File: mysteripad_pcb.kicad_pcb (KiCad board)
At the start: 2 copper layers, 76.2 x 146.6 mm, 74 parts, among them J1 PJ-320A, U1 ATmega328P-PU, Y1 Crystal

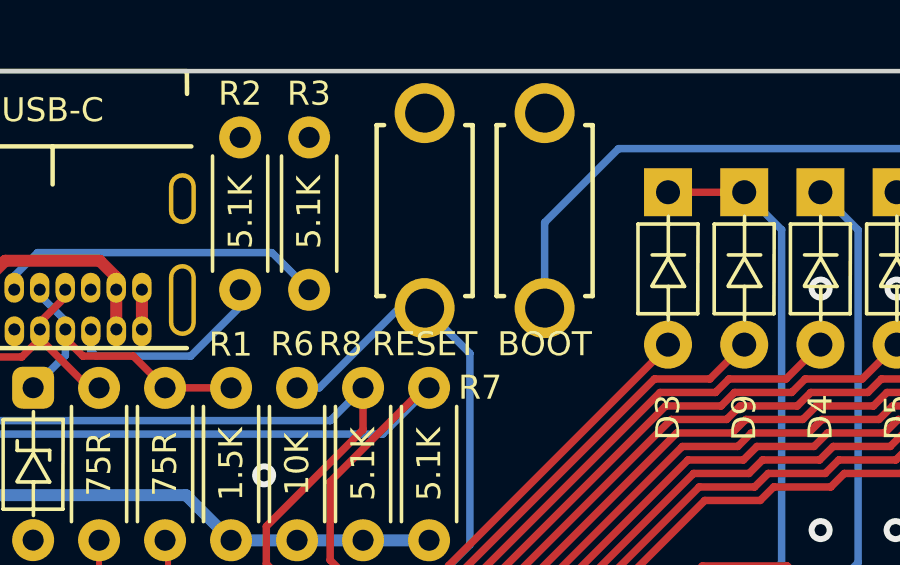
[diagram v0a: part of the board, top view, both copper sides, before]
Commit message: Fix RESET/BOOT silkscreen
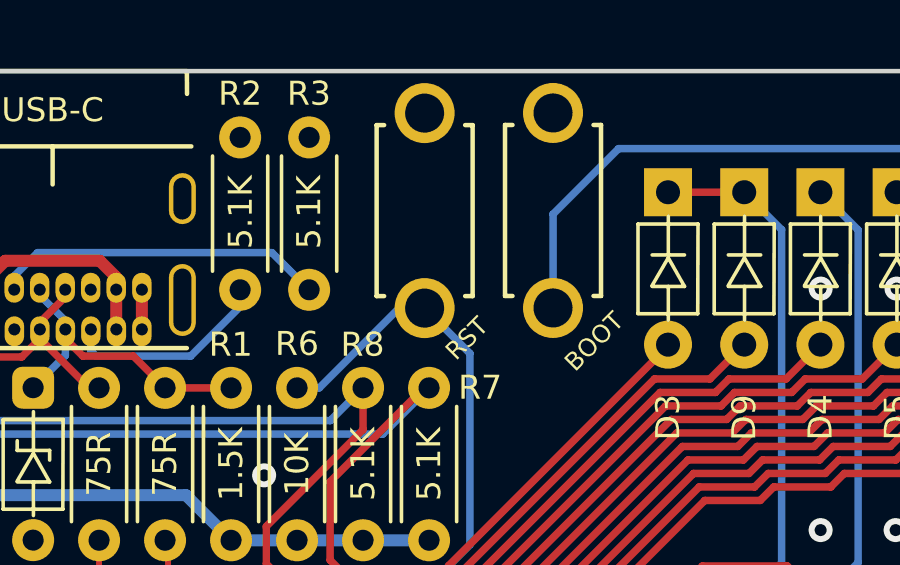
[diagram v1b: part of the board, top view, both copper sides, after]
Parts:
- RESET1: value RESET -> RST
- moved BOOT1 0.28 mm to (113.0, 34.6)
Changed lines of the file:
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@@
       (effects (font (size 1 1) (thickness 0.15)))
     )
-    (fp_text value "RESET" (at -4.45 0 180) (layer "F.SilkS")
-      (effects (font (size 0.8 0.8) (thickness 0.15)))
+    (fp_text value "RST" (at -4.2628 1.4098 225) (layer "F.SilkS")
+      (effects (font (size 0.6 0.6) (thickness 0.15)))
     )
     (fp_text user "RESET" (at 0 0 90) (layer "F.SilkS") hide
@@
     (property "Sheetname" "")
     (attr through_hole)
-    (fp_text reference "R8" (at 6.53895 -0.7542) (layer "F.SilkS")
+    (fp_text reference "R8" (at 6.52295 -0.0176) (layer "F.SilkS")
       (effects (font (size 0.8 0.8) (thickness 0.15)))
     )
@@
   )
   (footprint "kbd:ResetSW_1side" (layer "F.Cu")
-    (at 112.75 34.65 90)
+    (at 113.03 34.6456 90)
     (property "Sheetfile" "mysteripad_pcb.kicad_sch")
     (property "Sheetname" "")
@@
       (effects (font (size 1 1) (thickness 0.15)))
     )
-    (fp_text value "BOOT" (at -4.45 0 180) (layer "F.SilkS")
-      (effects (font (size 0.8 0.8) (thickness 0.15)))
+    (fp_text value "BOOT" (at -4.3688 1.3716 225) (layer "F.SilkS")
+      (effects (font (size 0.6 0.6) (thickness 0.15)))
     )
     (fp_text user "RESET" (at 0 0 90) (layer "F.SilkS") hide
@@
     (property "Sheetname" "")
     (attr through_hole)
-    (fp_text reference "R6" (at 6.53895 -0.1566) (layer "F.SilkS")
+    (fp_text reference "R6" (at 6.54835 -0.002) (layer "F.SilkS")
       (effects (font (size 0.8 0.8) (thickness 0.15)))
     )
@@
   (segment (start 95.948008 49.2134) (end 102.931612 49.2134) (width 0.25) (layer "B.Cu") (net 2))
   (segment (start 95.472608 48.738) (end 95.948008 49.2134) (width 0.25) (layer "B.Cu") (net 2))
-  (segment (start 112.75 37.9) (end 112.75 35.05) (width 0.25) (layer "B.Cu") (net 2))
+  (segment (start 125.569399 32.583999) (end 127.023 34.0376) (width 0.25) (layer "B.Cu") (net 2))
   (segment (start 105.259816 49.638) (end 106.221816 50.6) (width 0.25) (layer "B.Cu") (net 2))
+  (segment (start 113.03 34.77) (end 115.216001 32.583999) (width 0.25) (layer "B.Cu") (net 2))
   (segment (start 128.3 35.3146) (end 128.3 46.362751) (width 0.25) (layer "B.Cu") (net 2))
   (segment (start 125.892151 48.7706) (end 127.041903 47.620848) (width 0.25) (layer "B.Cu") (net 2))
   (segment (start 123.988547 48.7706) (end 125.892151 48.7706) (width 0.25) (layer "B.Cu") (net 2))
   (segment (start 128.3 46.362751) (end 127.041903 47.620848) (width 0.25) (layer "B.Cu") (net 2))
-  (segment (start 115.216001 32.583999) (end 125.569399 32.583999) (width 0.25) (layer "B.Cu") (net 2))
   (segment (start 121.634943 49.2206) (end 123.538547 49.2206) (width 0.25) (layer "B.Cu") (net 2))
   (segment (start 121.184943 49.6706) (end 121.634943 49.2206) (width 0.25) (layer "B.Cu") (net 2))
-  (segment (start 125.569399 32.583999) (end 127.023 34.0376) (width 0.25) (layer "B.Cu") (net 2))
   (segment (start 106.221816 50.6) (end 118.351939 50.6) (width 0.25) (layer "B.Cu") (net 2))
   (segment (start 82.266004 47.595) (end 83.409004 48.738) (width 0.25) (layer "B.Cu") (net 2))
   (segment (start 119.281339 49.6706) (end 121.184943 49.6706) (width 0.25) (layer "B.Cu") (net 2))
-  (segment (start 112.75 35.05) (end 115.216001 32.583999) (width 0.25) (layer "B.Cu") (net 2))
   (segment (start 83.409004 48.738) (end 95.472608 48.738) (width 0.25) (layer "B.Cu") (net 2))
   (segment (start 123.538547 49.2206) (end 123.988547 48.7706) (width 0.25) (layer "B.Cu") (net 2))
   (segment (start 118.351939 50.6) (end 119.281339 49.6706) (width 0.25) (layer "B.Cu") (net 2))
   (segment (start 127.023 34.0376) (end 128.3 35.3146) (width 0.25) (layer "B.Cu") (net 2))
+  (segment (start 113.03 37.8956) (end 113.03 34.77) (width 0.25) (layer "B.Cu") (net 2))
+  (segment (start 115.216001 32.583999) (end 125.569399 32.583999) (width 0.25) (layer "B.Cu") (net 2))
   (segment (start 102.931612 49.2134) (end 103.356212 49.638) (width 0.25) (layer "B.Cu") (net 2))
   (segment (start 103.356212 49.638) (end 105.259816 49.638) (width 0.25) (layer "B.Cu") (net 2))

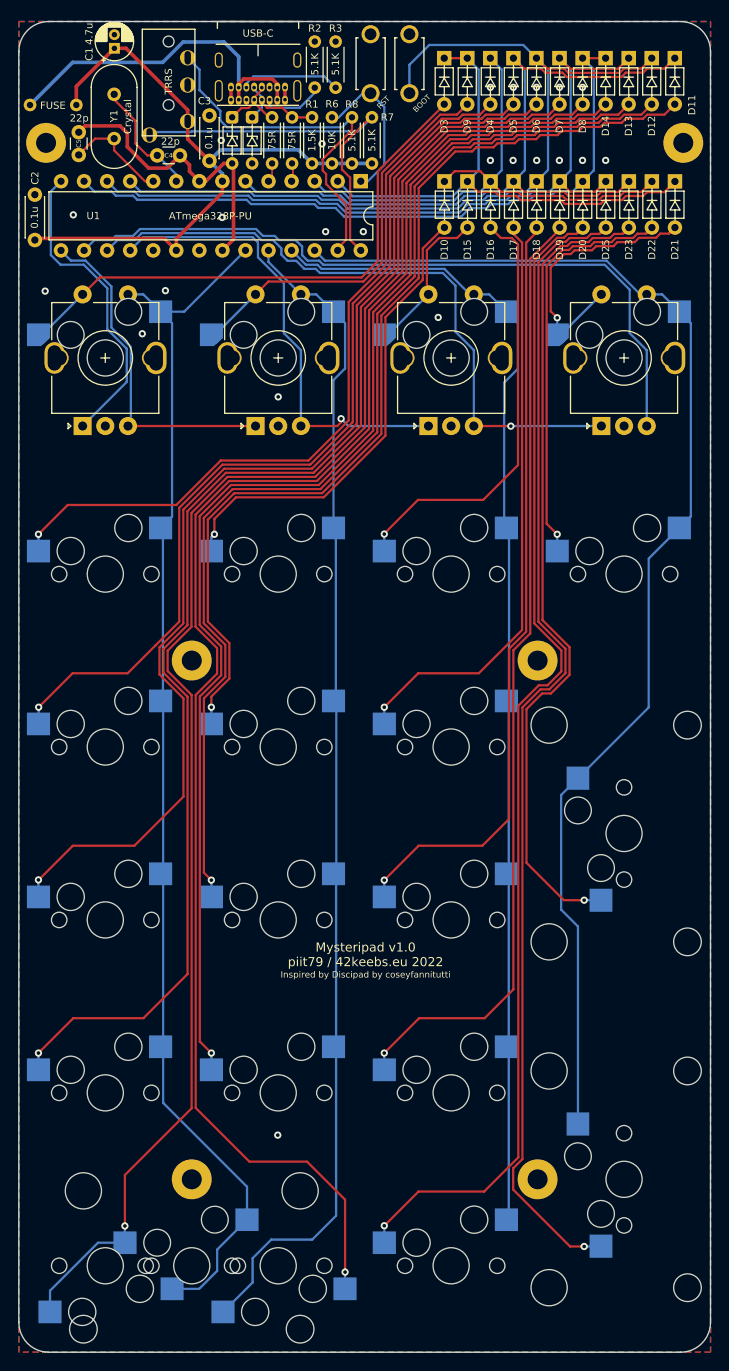
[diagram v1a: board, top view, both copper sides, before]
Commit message: Optimize routing for rounded tracks
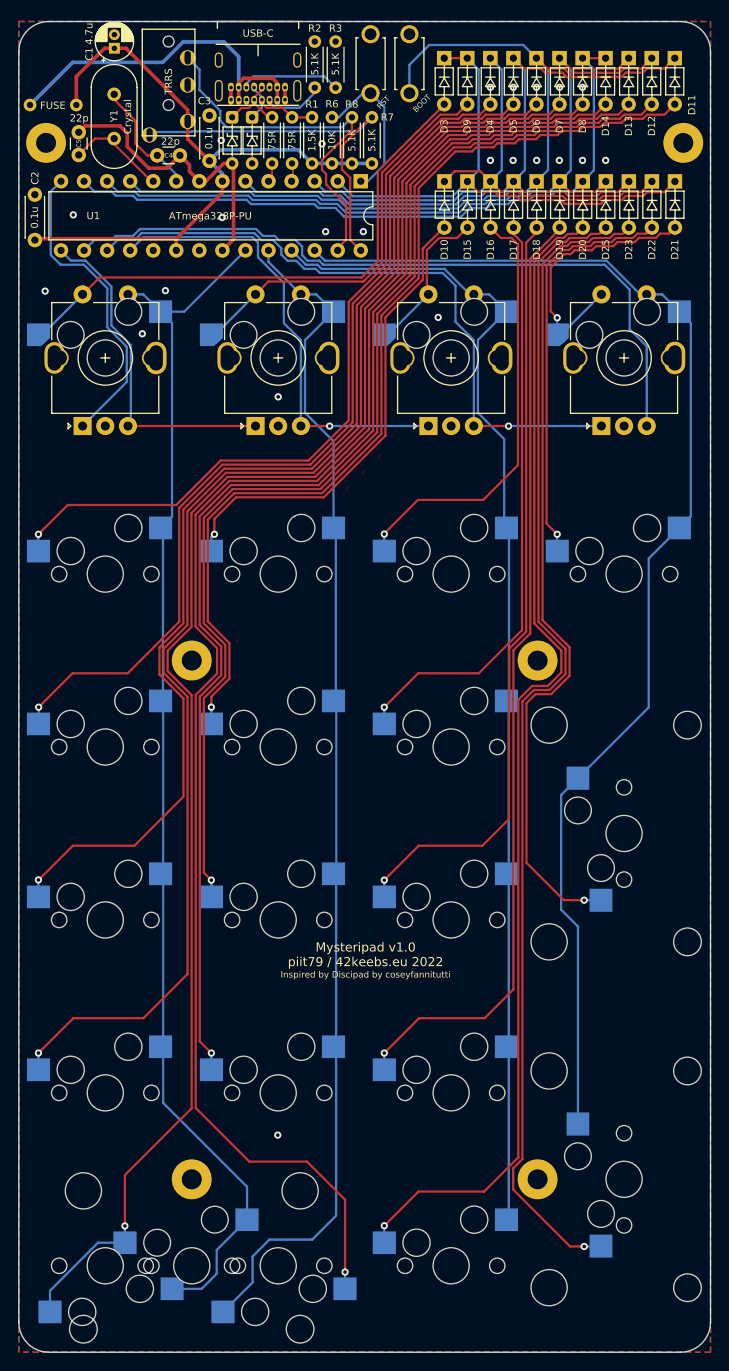
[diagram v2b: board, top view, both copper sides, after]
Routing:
- net col1: track 130.6 -> 132.3 mm
- net col2: track 128.6 -> 130.0 mm
- net EN3: track 52.0 -> 51.2 mm

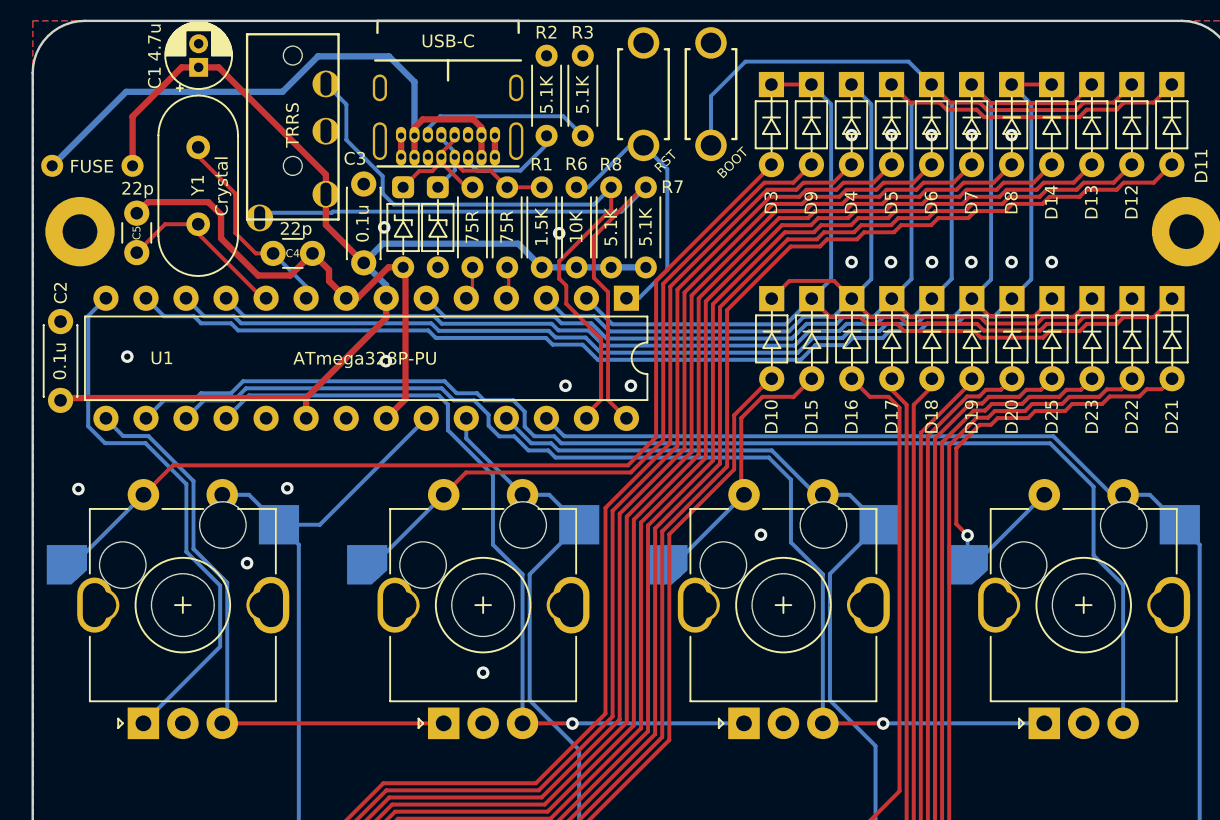
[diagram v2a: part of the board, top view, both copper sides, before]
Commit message: Move MCU and crystal down to avoid fix coutyard overlap
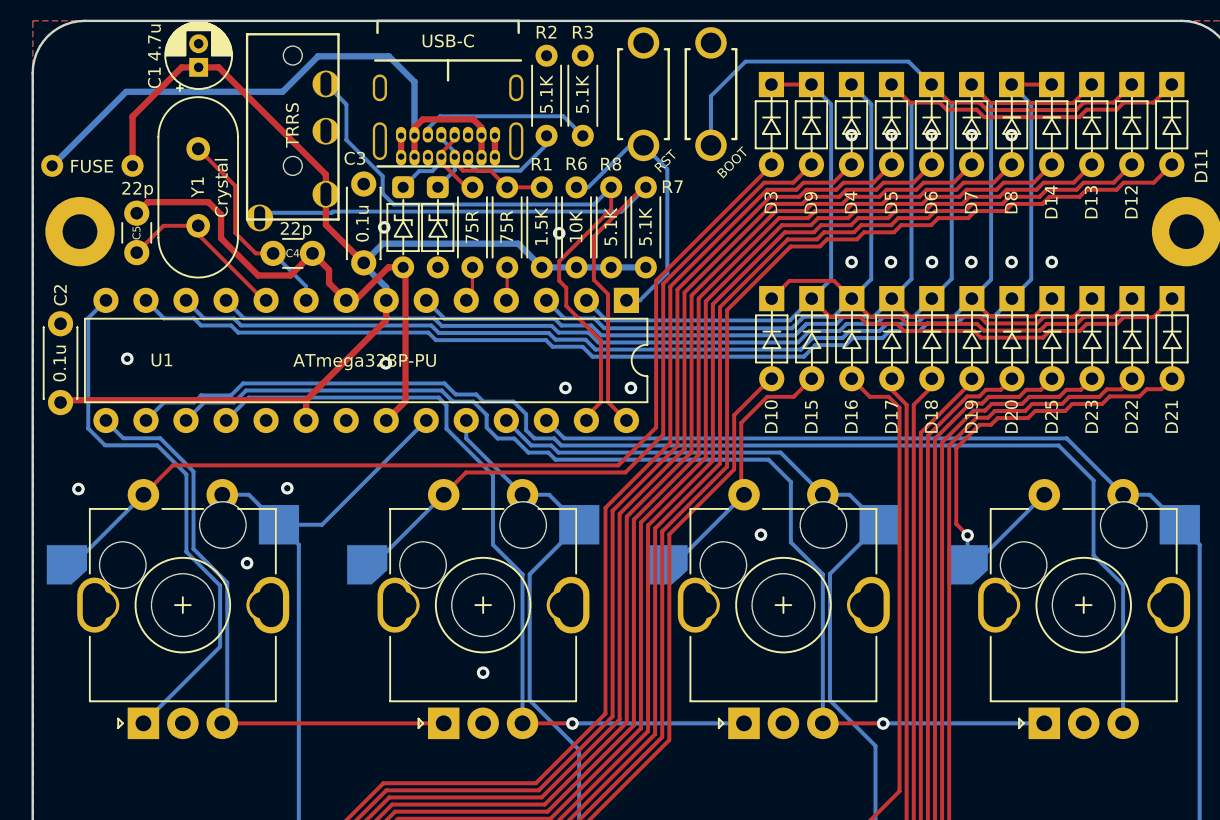
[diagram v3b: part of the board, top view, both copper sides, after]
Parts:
- moved U1 0.14 mm to (107.7, 47.7)
- moved C2 0.14 mm to (71.8, 54.2)
- moved Y1 0.10 mm to (80.5, 43.0)
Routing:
- net row2: track 79.8 -> 80.4 mm

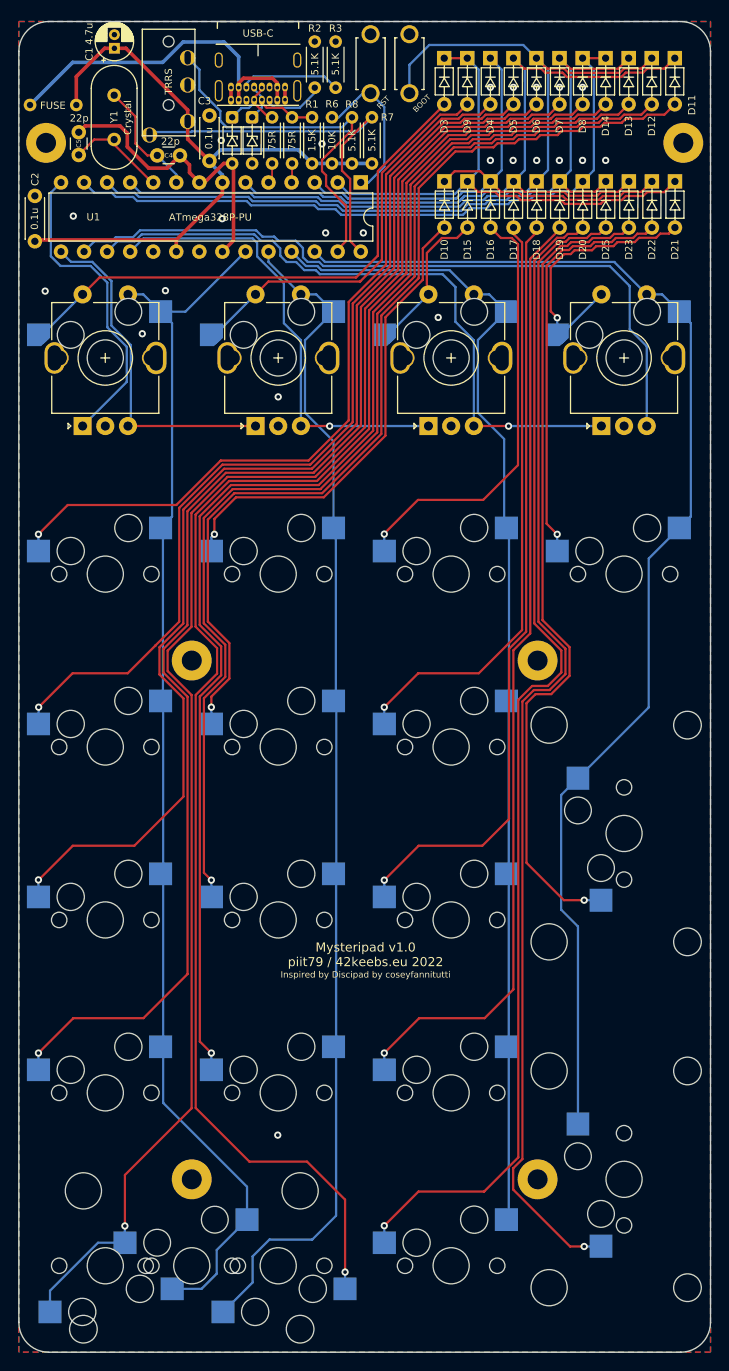
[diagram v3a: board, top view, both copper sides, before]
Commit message: Finish optimising routing for rounded traces
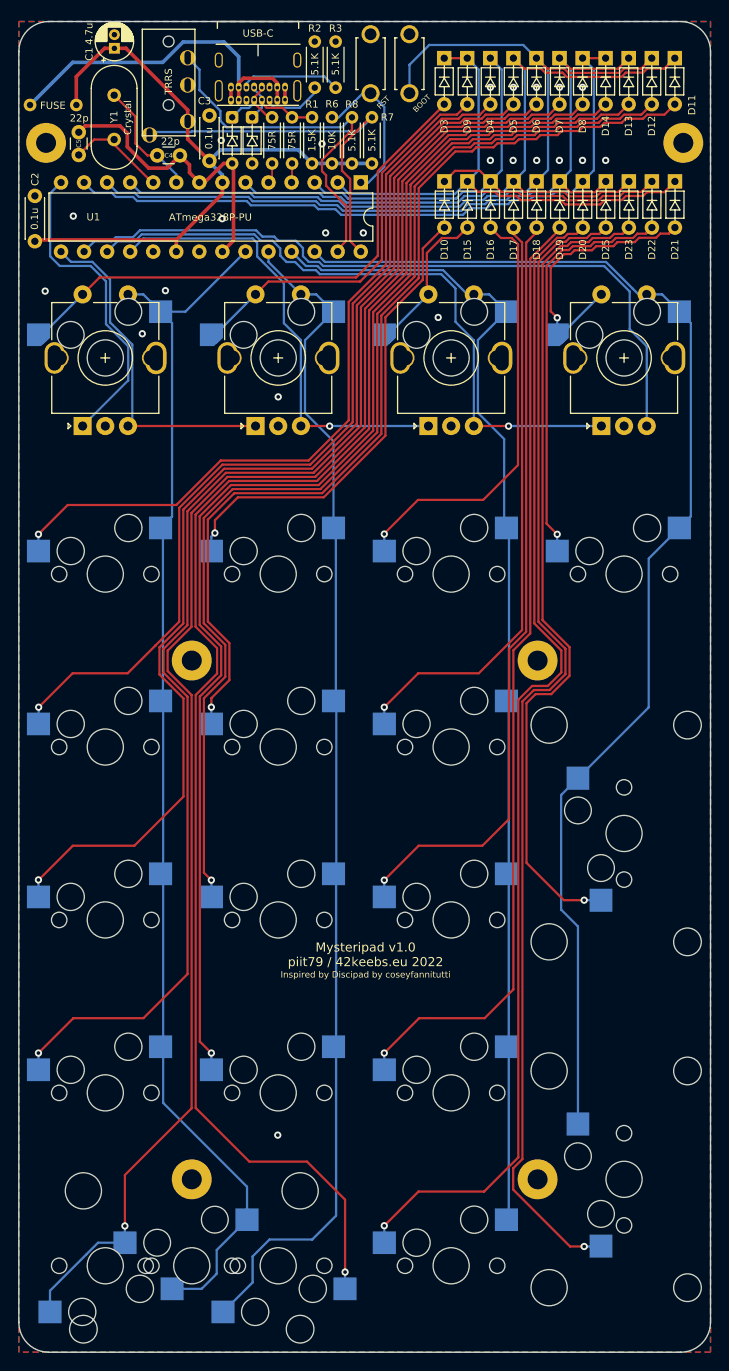
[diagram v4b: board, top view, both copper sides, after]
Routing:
- net row2: track 80.4 -> 79.6 mm

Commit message: Fix incorrect USB pullup; fix bottom mounting holes
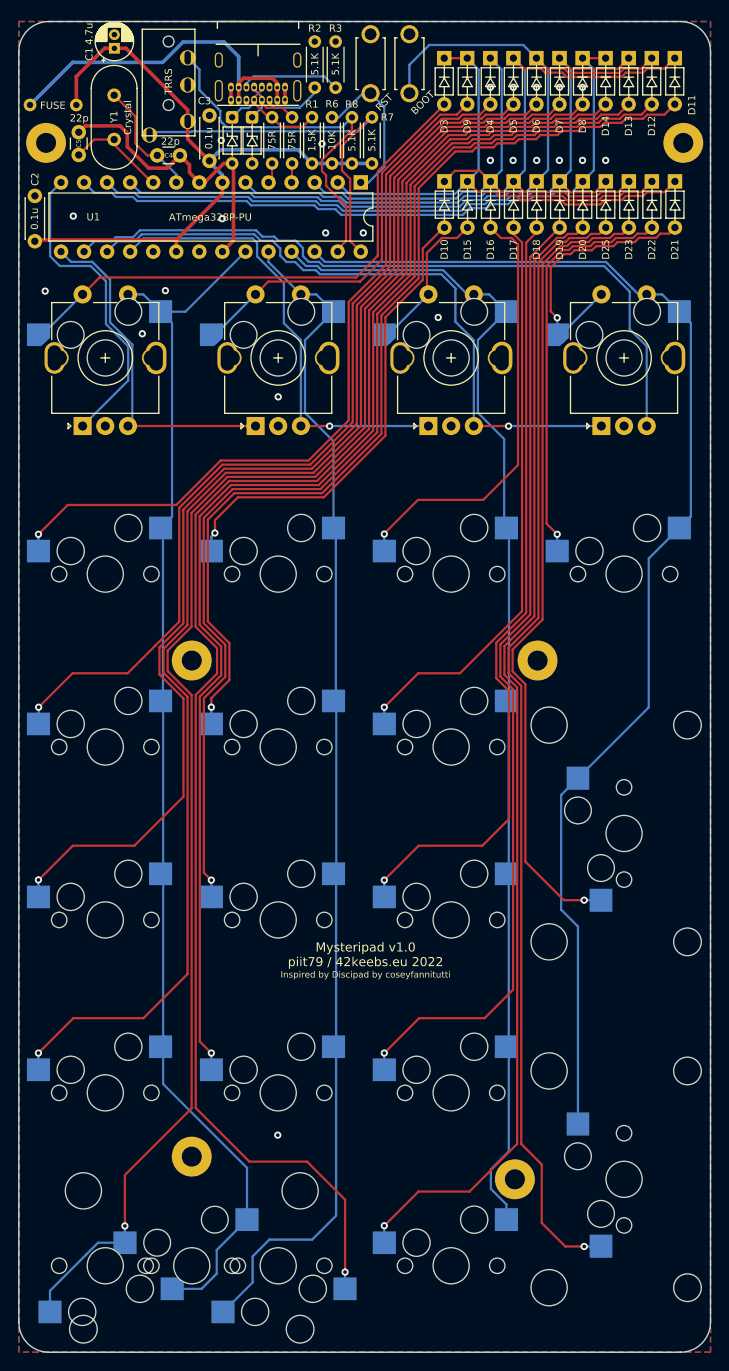
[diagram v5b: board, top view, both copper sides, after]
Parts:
- USB1: value USB-C -> USB_C_GCT_USB4085
- moved H5 2.50 mm to (89.1, 155.1)
- moved H6 2.50 mm to (124.7, 157.6)
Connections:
- R1 pad 2: Net-(D2-Pad1) -> Net-(D1-Pad1)
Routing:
- net Net-(D1-Pad1): track 8.10 -> 13.4 mm
- net Net-(D20-Pad2): track 129.6 -> 126.4 mm
- net Net-(D25-Pad2): track 128.1 -> 125.3 mm
- net Net-(D23-Pad2): track 91.3 -> 89.0 mm
- net Net-(D2-Pad1): track 10.6 -> 8.42 mm
- net col2: track 129.9 -> 131.4 mm
- net Net-(D17-Pad2): track 65.3 -> 64.1 mm
- net Net-(D19-Pad2): track 105.0 -> 106.2 mm
- net Net-(D18-Pad2): track 84.8 -> 86.0 mm
